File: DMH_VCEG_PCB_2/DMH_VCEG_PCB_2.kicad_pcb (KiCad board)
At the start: 2 copper layers, 148 x 139 mm, 224 parts, among them J21 Conn_01x10_PinHeader, J22 Conn_01x10_PinHeader, J23 Conn_01x10_PinHeader, J24 Conn_01x06_PinHeader, J25 Conn_01x10_PinHeader, J26 Conn_01x10_PinHeader, J27 Conn_01x10_PinHeader, Q10 BC548, Q11 BC558, Q12 BC558, Q13 BC548, Q14 BC548, Q15 BC548, Q16 BC548, Q23 BC548, Q24 BC548, Q25 BC548, Q26 BC548, Q27 BC558, Q28 BC558, Q29 BC548, Q30 BC548, Q31 BC548, Q32 BC548, Q7 BC548, Q8 BC548, Q9 BC548, SW1 DPDT_OnOff(On), SW2 DPDT_OnOffOn, SW3 SPDT_OnOn, SW4 DPDT_OnOffOn, SW5 DPDT_OnOff(On), U10 TL074, U14 CD4066BE, U18 TL074, U19 TL074, U20 TL074, U21 TL074, U22 CD4066BE, U23 TL074, U24 CD4066BE, U4 CD4066BE, U8 TL074, U9 TL074

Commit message: PCB 2 routing in progress
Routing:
- net /CV Processing A/Rel CV: track 0.00 -> 97.1 mm
- net Net-(U21B--): track 0.00 -> 96.3 mm, vias 0 -> 1
- net /CV Processing A/Att CV: track 15.5 -> 106.0 mm, vias 0 -> 1
- net Net-(U21A--): track 0.00 -> 84.2 mm, vias 0 -> 1
- net /CV Processing A/Dec CV: track 0.00 -> 83.9 mm
- net Net-(J22D-Pin_4): track 0.00 -> 78.6 mm
- net Net-(J23C-Pin_3): track 0.00 -> 74.5 mm
- net /Core Circuit A/Sus_State: track 0.00 -> 68.0 mm
- net Net-(U21D--): track 0.00 -> 67.6 mm
- net /Core Circuit A/Att_State: track 0.00 -> 58.7 mm
- net /Core Circuit A/Rel_State: track 0.00 -> 57.6 mm
- net Net-(U21B-+): track 0.00 -> 56.5 mm
- net Net-(U8C--): track 0.00 -> 54.5 mm
- net /CV Processing A/Rel Proc CV: track 0.00 -> 51.5 mm
- net Net-(D17-K): track 2.54 -> 53.7 mm
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
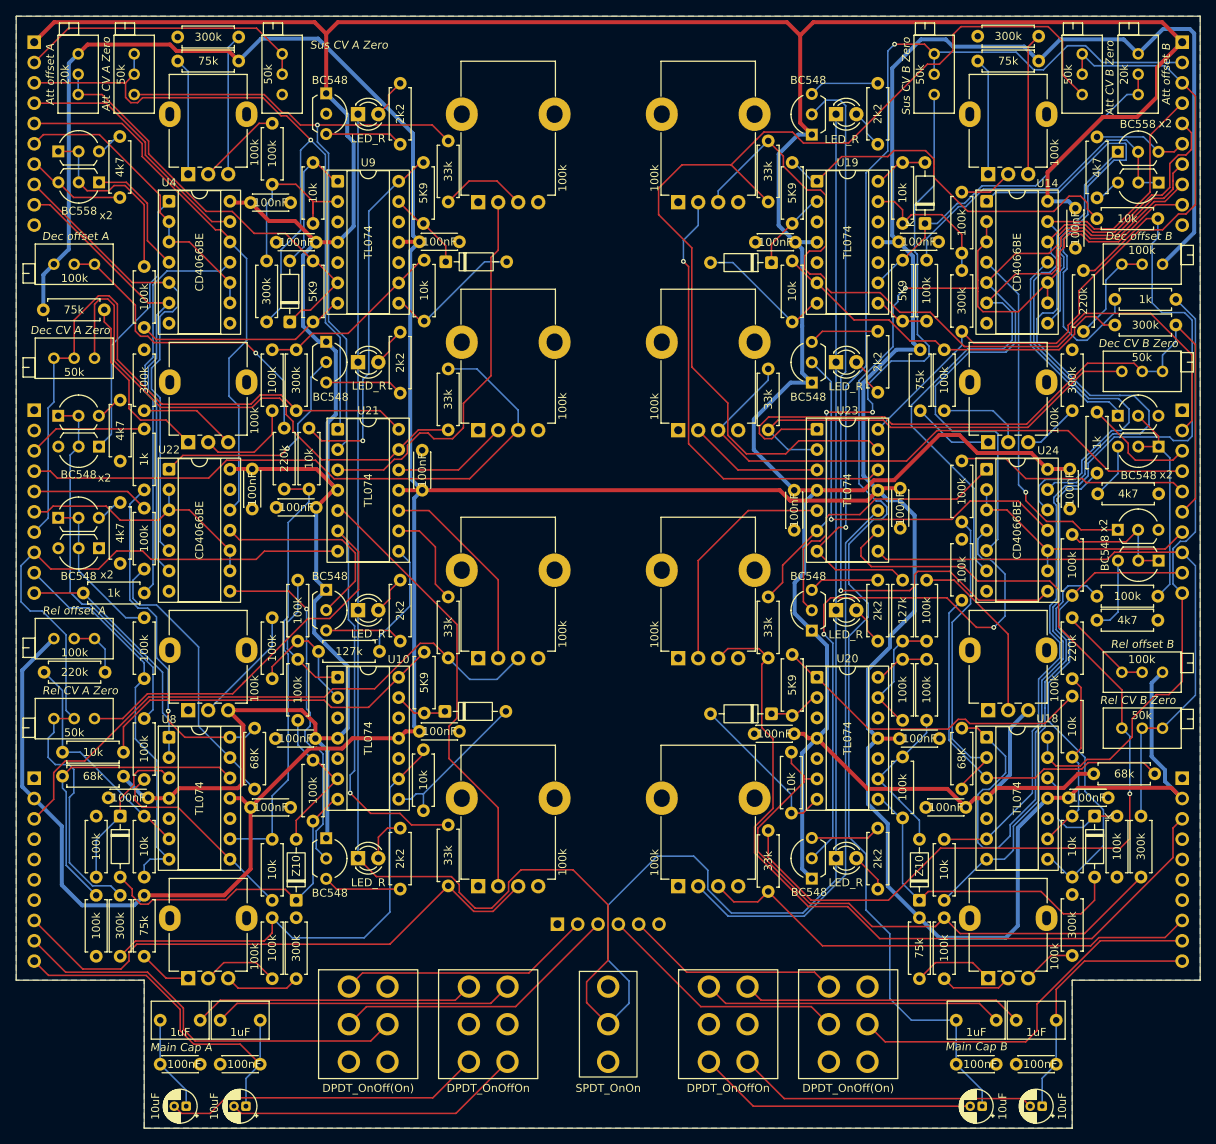
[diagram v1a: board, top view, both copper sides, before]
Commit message: PCB 2 Routing complete
But still need optimization for empty areas
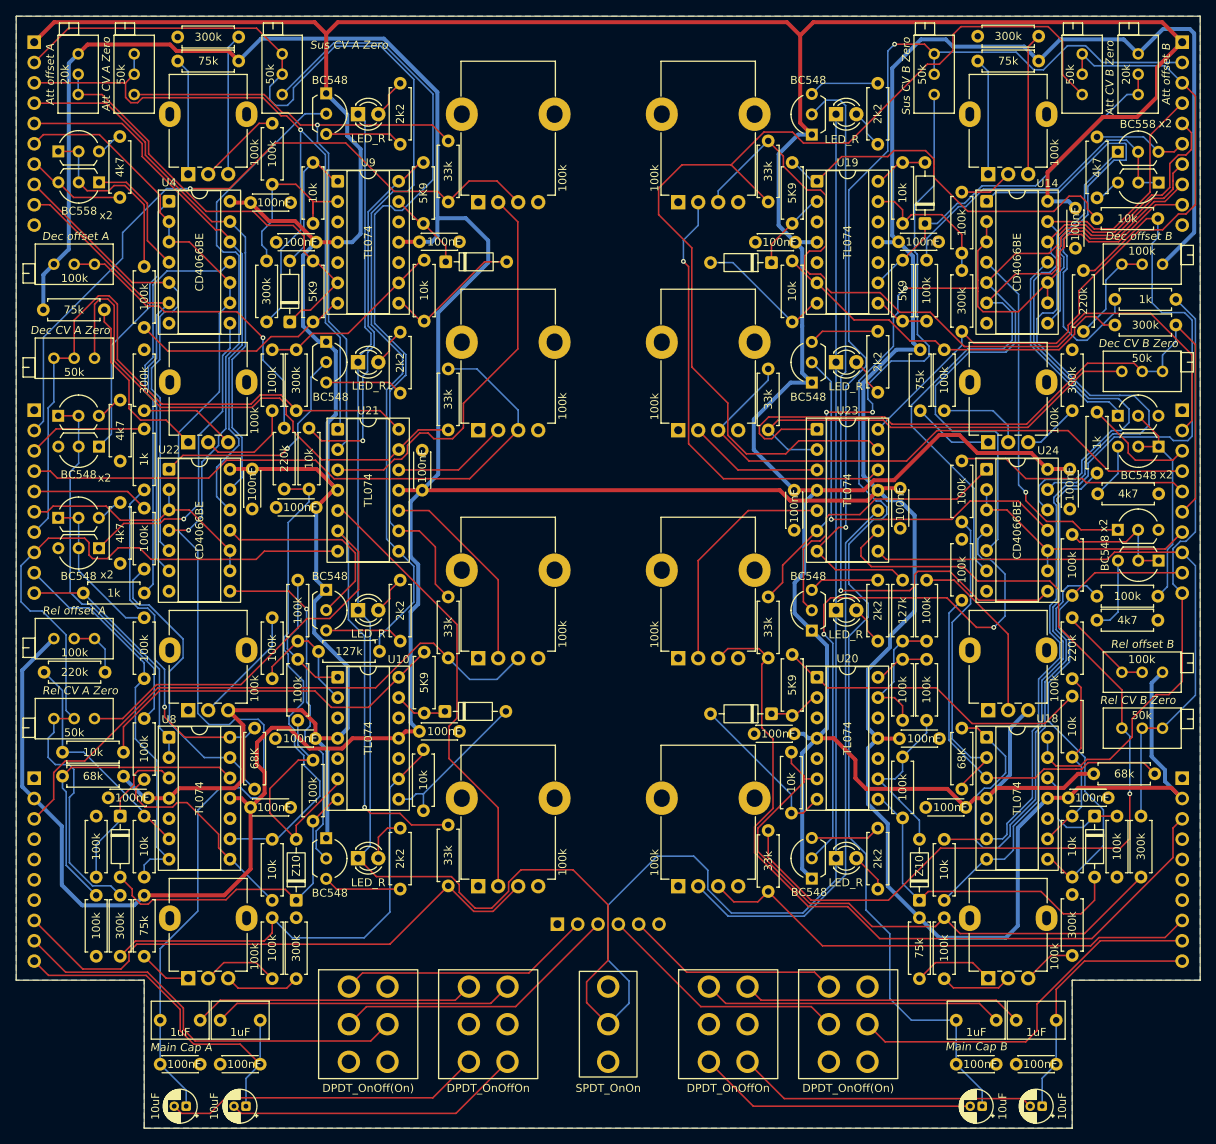
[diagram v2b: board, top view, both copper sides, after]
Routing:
- net Net-(J21F-Pin_6): track 50.0 -> 161.2 mm
- net /CV Processing A/Sus CV: track 51.3 -> 144.8 mm
- net Net-(U21C--): track 12.3 -> 99.3 mm
- net Net-(J22B-Pin_2): track 10.9 -> 88.6 mm, vias 0 -> 1
- net Net-(Q7-B): track 0.00 -> 66.4 mm, vias 0 -> 1
- net /CV Processing A/Rel Cur Snk: track 0.00 -> 39.0 mm, vias 0 -> 1
- net /Core Circuit A/Dec_State: track 31.5 -> 67.7 mm
- net -12V: track 592.0 -> 617.9 mm
- net Net-(D19-A): track 19.5 -> 30.1 mm
- net Net-(U8C--): track 54.5 -> 59.6 mm
- net +12V: track 586.4 -> 589.3 mm
- net Net-(U8D--): track 35.6 -> 38.4 mm
- net /Core Circuit A/LEDs SW: track 298.9 -> 301.5 mm
- net Net-(U21A-+): track 49.1 -> 51.1 mm
- net /CV Processing B/Sus CV: track 122.2 -> 124.0 mm
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
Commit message: Finished PCB 2 routing optimization
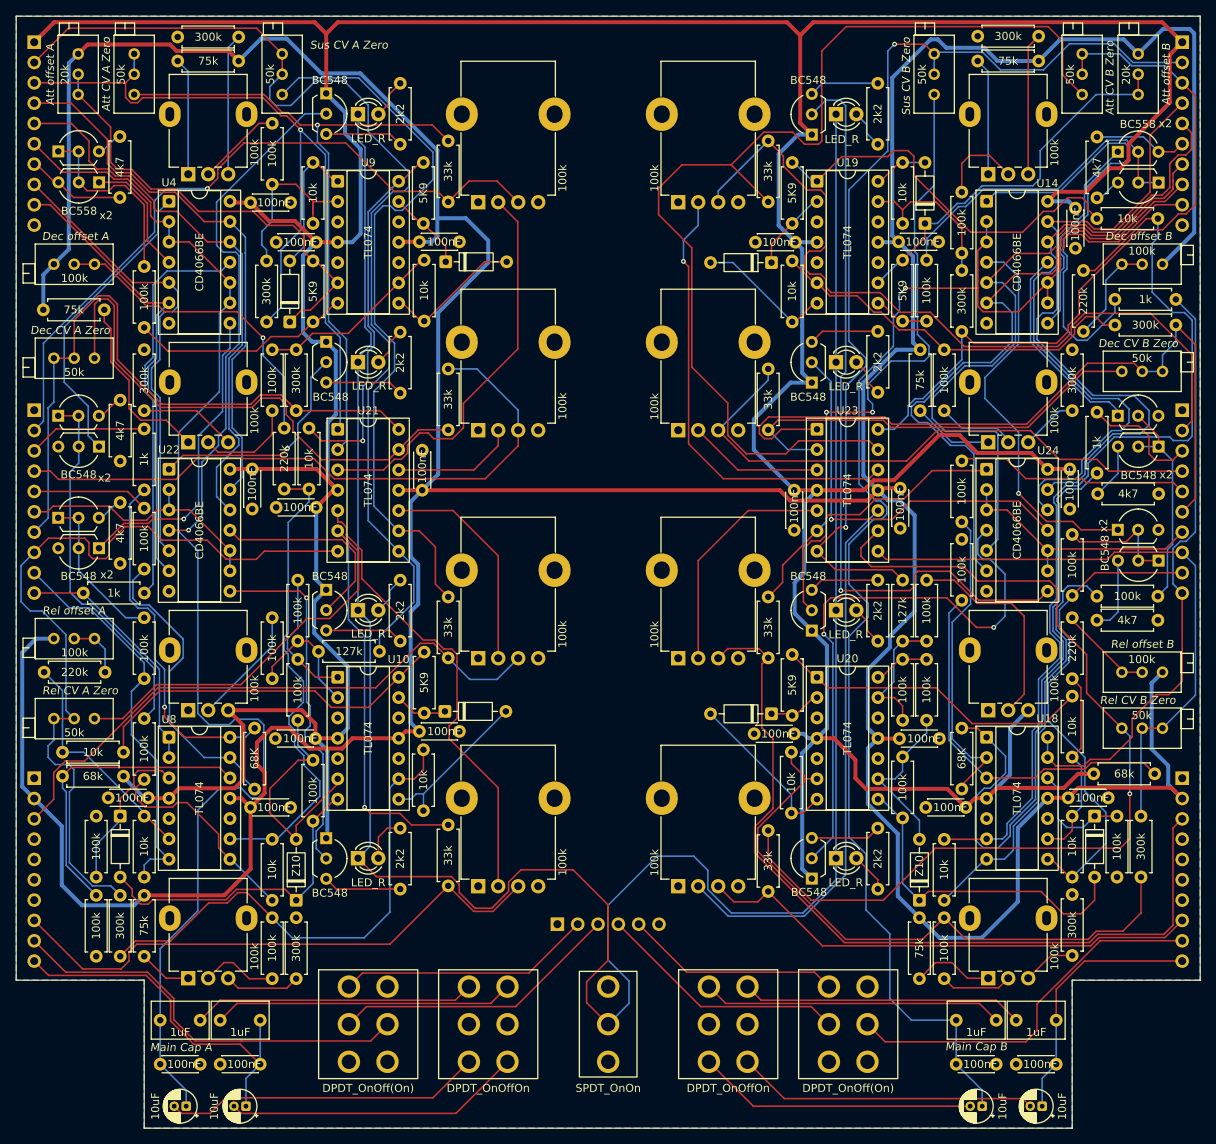
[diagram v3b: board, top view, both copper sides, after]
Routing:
- net /CV Processing A/Sus CV: track 144.8 -> 134.9 mm
- net Net-(U21C--): track 99.3 -> 91.9 mm
- net Net-(U23D--): track 131.5 -> 137.0 mm
- net -12V: track 617.9 -> 612.5 mm
- net Net-(J27C-Pin_3): track 99.7 -> 105.1 mm
- net /CV Processing B/Rel Cur Snk: track 44.8 -> 49.6 mm
- net Net-(U20B--): track 73.1 -> 77.6 mm
- net Net-(R169-Pad1): track 22.5 -> 26.6 mm
- net Net-(R150-Pad1): track 6.73 -> 10.8 mm
- net /CV Processing A/Dec Cur Snk: track 34.3 -> 37.9 mm
- net /CV Processing A/Rel CV: track 98.8 -> 101.9 mm
- net Net-(U10C--): track 61.2 -> 63.9 mm
- net Net-(D36-K): track 45.9 -> 47.9 mm
- net Net-(R157-Pad2): track 47.5 -> 49.6 mm
- net Net-(U21C-+): track 25.8 -> 27.6 mm
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
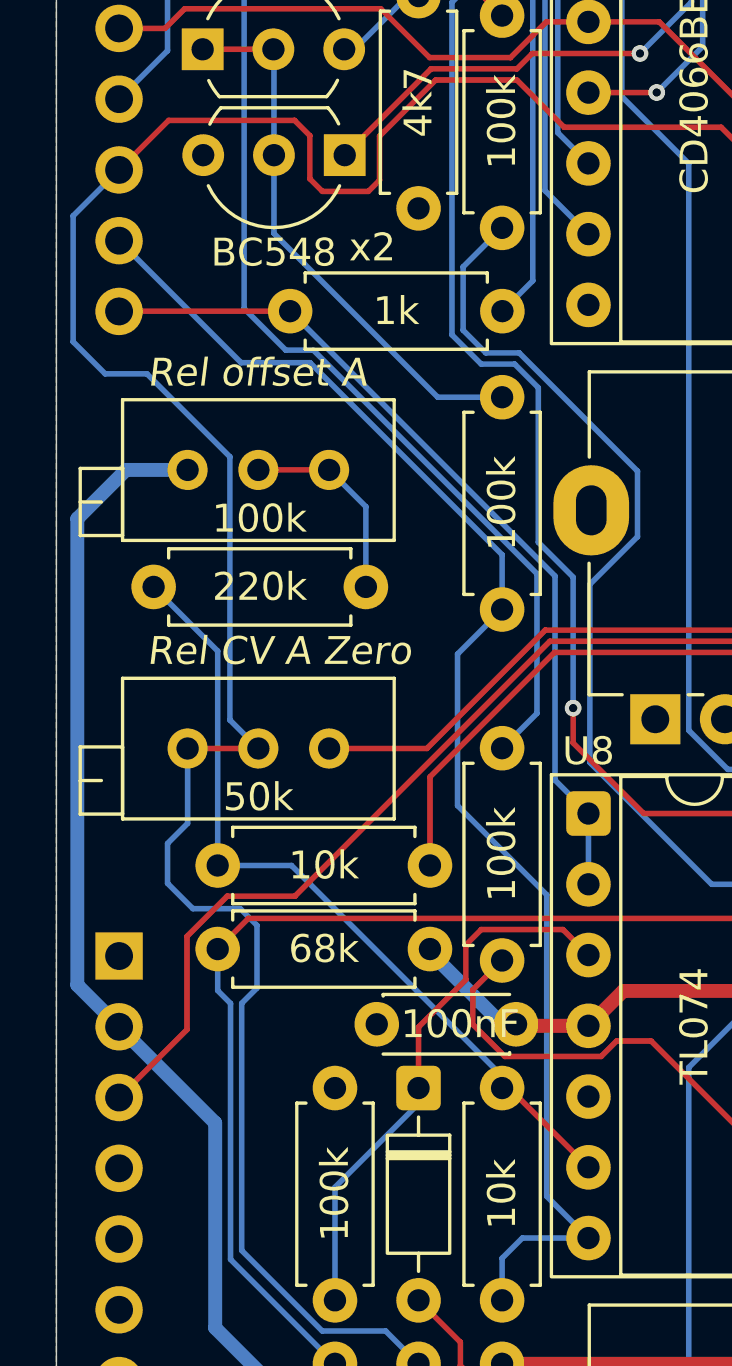
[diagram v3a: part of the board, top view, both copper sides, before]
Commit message: Synced PCB 2 schematic to PCB 1
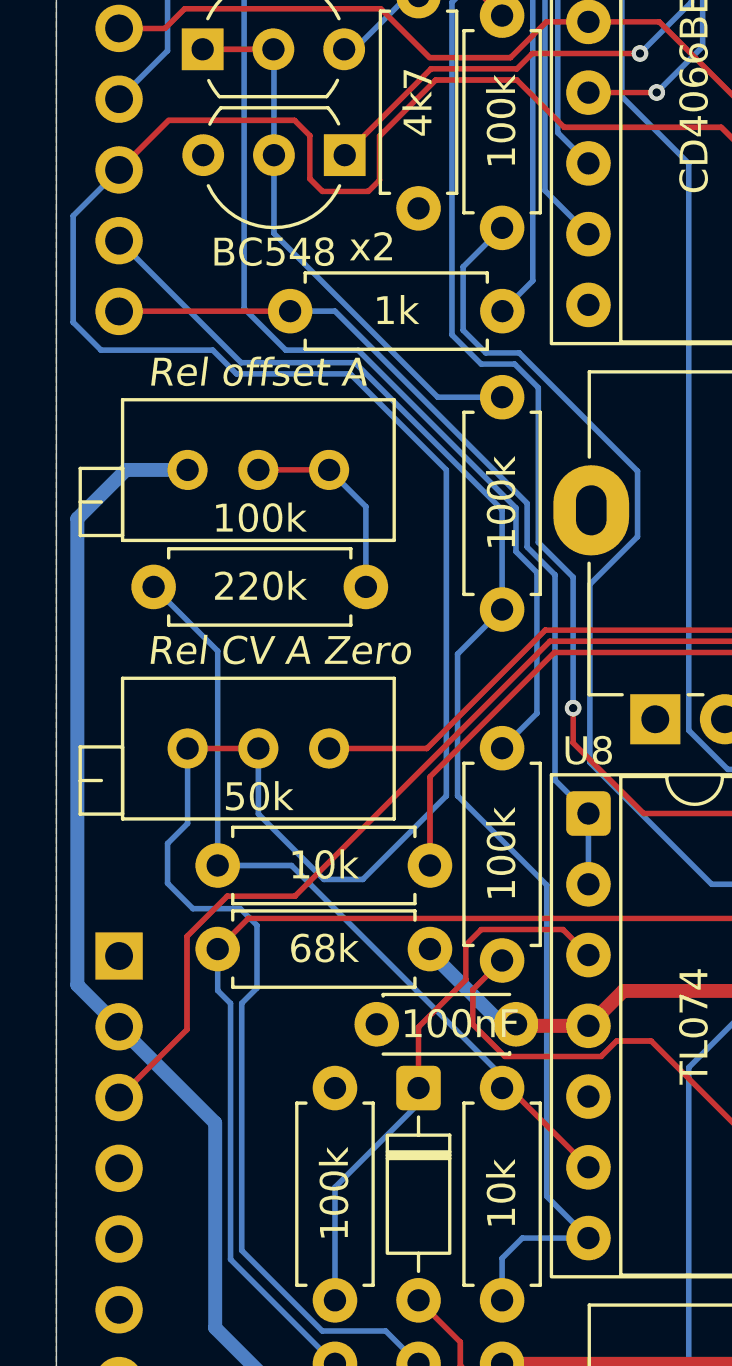
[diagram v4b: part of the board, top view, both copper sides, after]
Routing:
- net /CV Processing A/Rel CV: track 101.9 -> 121.6 mm
- net Net-(Q13-B): track 46.3 -> 47.2 mm
- net /CV Processing A/Rel Proc CV: track 50.5 -> 51.4 mm
- net /CV Processing A/Sus Level: track 31.2 -> 32.1 mm
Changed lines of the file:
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@@
 	)
 	(segment
-		(start 34.23295 116)
-		(end 32.739 114.50605)
+		(start 42.498 121.6651)
+		(end 36.8329 116)
 		(width 0.2)
 		(layer "B.Cu")
@@
 	)
 	(segment
-		(start 43.25 124.0271)
-		(end 35.2229 116)
+		(start 33.81 98.39)
+		(end 33.81 96.3)
 		(width 0.2)
 		(layer "B.Cu")
@@
 	)
 	(segment
-		(start 33.81 98.39)
-		(end 33.81 96.3)
+		(start 32.739 99.461)
+		(end 33.81 98.39)
 		(width 0.2)
 		(layer "B.Cu")
@@
 	)
 	(segment
-		(start 35.2229 116)
-		(end 34.23295 116)
+		(start 34.23295 116)
+		(end 32.739 114.50605)
 		(width 0.2)
 		(layer "B.Cu")
@@
 	(segment
 		(start 43.25 129.04)
-		(end 43.25 124.0271)
+		(end 43.25 123.9842)
 		(width 0.2)
 		(layer "B.Cu")
@@
 	)
 	(segment
-		(start 32.739 99.461)
-		(end 33.81 98.39)
+		(start 42.498 123.2322)
+		(end 42.498 121.6651)
+		(width 0.2)
+		(layer "B.Cu")
+		(net 48)
+	)
+	(segment
+		(start 36.8329 116)
+		(end 34.23295 116)
+		(width 0.2)
+		(layer "B.Cu")
+		(net 48)
+	)
+	(segment
+		(start 43.25 123.9842)
+		(end 42.498 123.2322)
 		(width 0.2)
 		(layer "B.Cu")
@@
 	)
 	(segment
-		(start 26.601 111.179)
-		(end 28.25 109.53)
+		(start 35.54395 151.211)
+		(end 32.652 148.31905)
 		(width 0.2)
 		(layer "B.Cu")
@@
 	)
 	(segment
-		(start 35.54395 151.211)
-		(end 32.652 148.31905)
+		(start 28.25 109.53)
+		(end 26.601 111.179)
 		(width 0.2)
 		(layer "B.Cu")
@@
 	)
 	(segment
-		(start 27.75 116.85)
-		(end 26.601 115.701)
+		(start 31.6129 116)
+		(end 32.4639 116.851)
 		(width 0.2)
 		(layer "B.Cu")
@@
 	)
 	(segment
-		(start 32.229 119.829)
-		(end 29.25 116.85)
+		(start 39.999 120.3003)
+		(end 39.999 132.001)
 		(width 0.2)
 		(layer "B.Cu")
@@
 	)
 	(segment
-		(start 33.25 130.3)
-		(end 32.229 129.279)
+		(start 26.601 111.179)
+		(end 26.601 115.001)
 		(width 0.2)
 		(layer "B.Cu")
@@
 	)
 	(segment
+		(start 37 135)
+		(end 35.6 135)
+		(width 0.2)
+		(layer "B.Cu")
+		(net 92)
+	)
+	(segment
 		(start 32.652 139.448)
 		(end 33.2 138.9)
@@
 	)
 	(segment
+		(start 33.25 132.65)
+		(end 33.25 130.3)
+		(width 0.2)
+		(layer "B.Cu")
+		(net 92)
+	)
+	(segment
+		(start 32.4639 116.851)
+		(end 36.5497 116.851)
+		(width 0.2)
+		(layer "B.Cu")
+		(net 92)
+	)
+	(segment
 		(start 30.9 136.05)
 		(end 29.990001 135.140001)
@@
 	)
 	(segment
+		(start 35.6 135)
+		(end 33.25 132.65)
+		(width 0.2)
+		(layer "B.Cu")
+		(net 92)
+	)
+	(segment
 		(start 39 152.39)
 		(end 37.821 151.211)
@@
 	)
 	(segment
-		(start 29.25 116.85)
-		(end 27.75 116.85)
+		(start 26.601 115.001)
+		(end 27.6 116)
 		(width 0.2)
 		(layer "B.Cu")
@@
 	)
 	(segment
-		(start 26.601 115.701)
-		(end 26.601 111.179)
+		(start 27.6 116)
+		(end 31.6129 116)
 		(width 0.2)
 		(layer "B.Cu")
@@
 	)
 	(segment
-		(start 32.229 129.279)
-		(end 32.229 119.829)
+		(start 36.5497 116.851)
+		(end 39.999 120.3003)
 		(width 0.2)
 		(layer "B.Cu")
@@
 	)
 	(segment
+		(start 39.999 132.001)
+		(end 37 135)
+		(width 0.2)
+		(layer "B.Cu")
+		(net 92)
+	)
+	(segment
 		(start 170.58 98)
 		(end 168.398 98)
@@
 	)
 	(segment
-		(start 42 150.11)
-		(end 42 148.6)
+		(start 43.601 135.201)
+		(end 43.601 146.376)
 		(width 0.2)
 		(layer "B.Cu")
@@
 	)
 	(segment
-		(start 40.4 132.35)
-		(end 43.601 135.551)
+		(start 42 150.11)
+		(end 42 148.6)
 		(width 0.2)
 		(layer "B.Cu")
@@
 	)
 	(segment
-		(start 42 125.31)
-		(end 40.4 126.91)
+		(start 36.7158 116.45)
+		(end 32.63 116.45)
 		(width 0.2)
 		(layer "B.Cu")
@@
 	)
 	(segment
-		(start 40.4 126.91)
-		(end 40.4 132.35)
+		(start 32.63 116.45)
+		(end 28.25 112.07)
 		(width 0.2)
 		(layer "B.Cu")
@@
 	)
 	(segment
-		(start 42.725 147.875)
-		(end 45.1 147.875)
+		(start 42 125.31)
+		(end 40.4 126.91)
 		(width 0.2)
 		(layer "B.Cu")
@@
 	)
 	(segment
-		(start 42 125.31)
-		(end 42 123.3442)
+		(start 40.4 126.91)
+		(end 40.4 132)
 		(width 0.2)
 		(layer "B.Cu")
@@
 	)
 	(segment
-		(start 42 148.6)
-		(end 42.725 147.875)
+		(start 42 125.31)
+		(end 42 121.7342)
 		(width 0.2)
 		(layer "B.Cu")
@@
 	)
 	(segment
-		(start 43.601 135.551)
-		(end 43.601 146.376)
+		(start 43.601 146.376)
+		(end 45.1 147.875)
 		(width 0.2)
 		(layer "B.Cu")
@@
 	)
 	(segment
-		(start 43.601 146.376)
-		(end 45.1 147.875)
+		(start 42 121.7342)
+		(end 36.7158 116.45)
 		(width 0.2)
 		(layer "B.Cu")
@@
 	)
 	(segment
-		(start 32.63 116.45)
-		(end 28.25 112.07)
+		(start 42.725 147.875)
+		(end 45.1 147.875)
 		(width 0.2)
 		(layer "B.Cu")
@@
 	)
 	(segment
-		(start 42 123.3442)
-		(end 35.1058 116.45)
+		(start 42 148.6)
+		(end 42.725 147.875)
 		(width 0.2)
 		(layer "B.Cu")
@@
 	)
 	(segment
-		(start 35.1058 116.45)
-		(end 32.63 116.45)
+		(start 40.4 132)
+		(end 43.601 135.201)
 		(width 0.2)
 		(layer "B.Cu")
@@
 	)
 	(segment
+		(start 43.9 131.435)
+		(end 43.9 124.0671)
+		(width 0.2)
+		(layer "B.Cu")
+		(net 106)
+	)
+	(segment
+		(start 42.899 121.499)
+		(end 36 114.6)
+		(width 0.2)
+		(layer "B.Cu")
+		(net 106)
+	)
+	(segment
+		(start 43.9 124.0671)
+		(end 42.899 123.0661)
+		(width 0.2)
+		(layer "B.Cu")
+		(net 106)
+	)
+	(segment
 		(start 45.1 135.175)
 		(end 45.1 132.635)
@@
 	)
 	(segment
-		(start 43.9 131.435)
-		(end 43.9 124.11)
+		(start 42.899 123.0661)
+		(end 42.899 121.499)
 		(width 0.2)
 		(layer "B.Cu")
@@
 	)
 	(segment
-		(start 43.9 124.11)
+		(start 36 114.6)
 		(end 34.39 114.6)
 		(width 0.2)
